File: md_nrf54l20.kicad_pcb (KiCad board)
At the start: 4 copper layers, 43.2 x 17.8 mm, 42 parts, among them J10 Conn_01x15, J5 USB_C, J7 JST SH I2C, J9 Conn_01x15, SW1 RESET, U1 nRF54L20, U2 AMS1117-3.3, U3 CH347T, U4 M6017-02, Y1 8MHz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

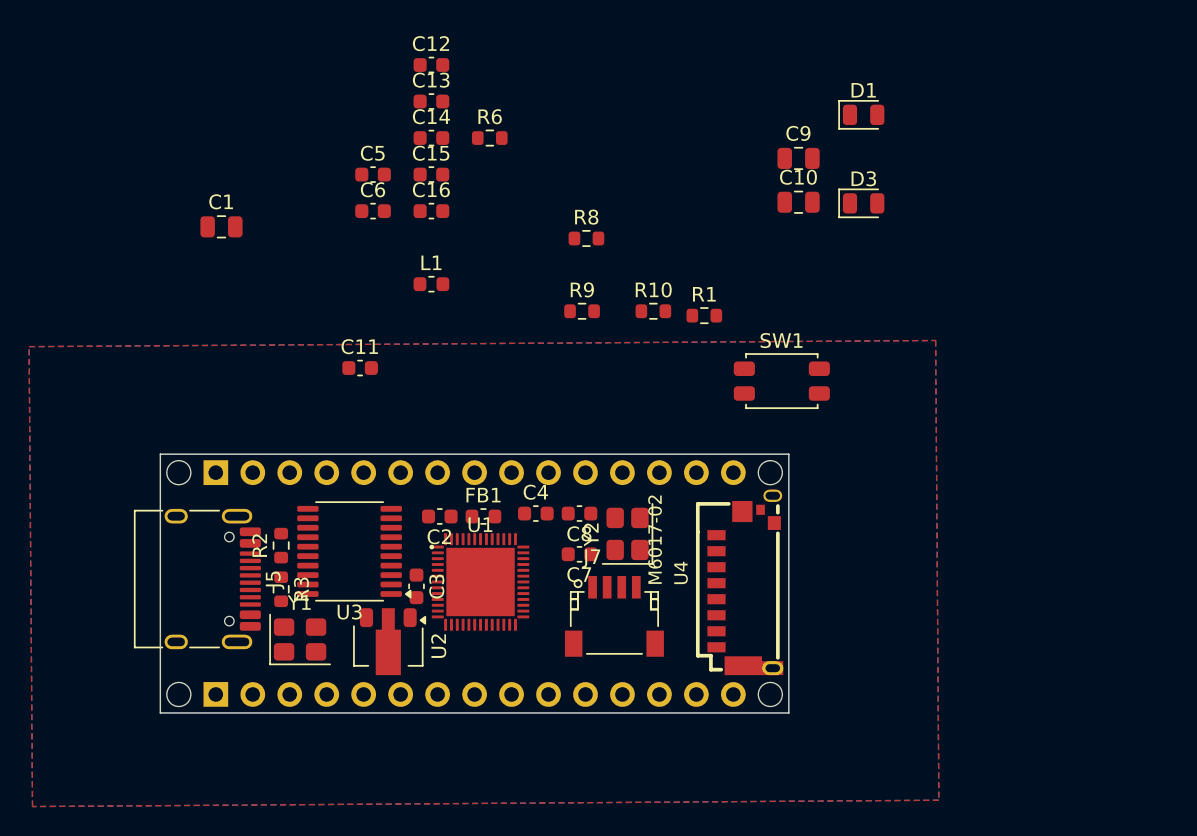
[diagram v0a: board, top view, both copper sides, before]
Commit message: Remove 10uf filter cap
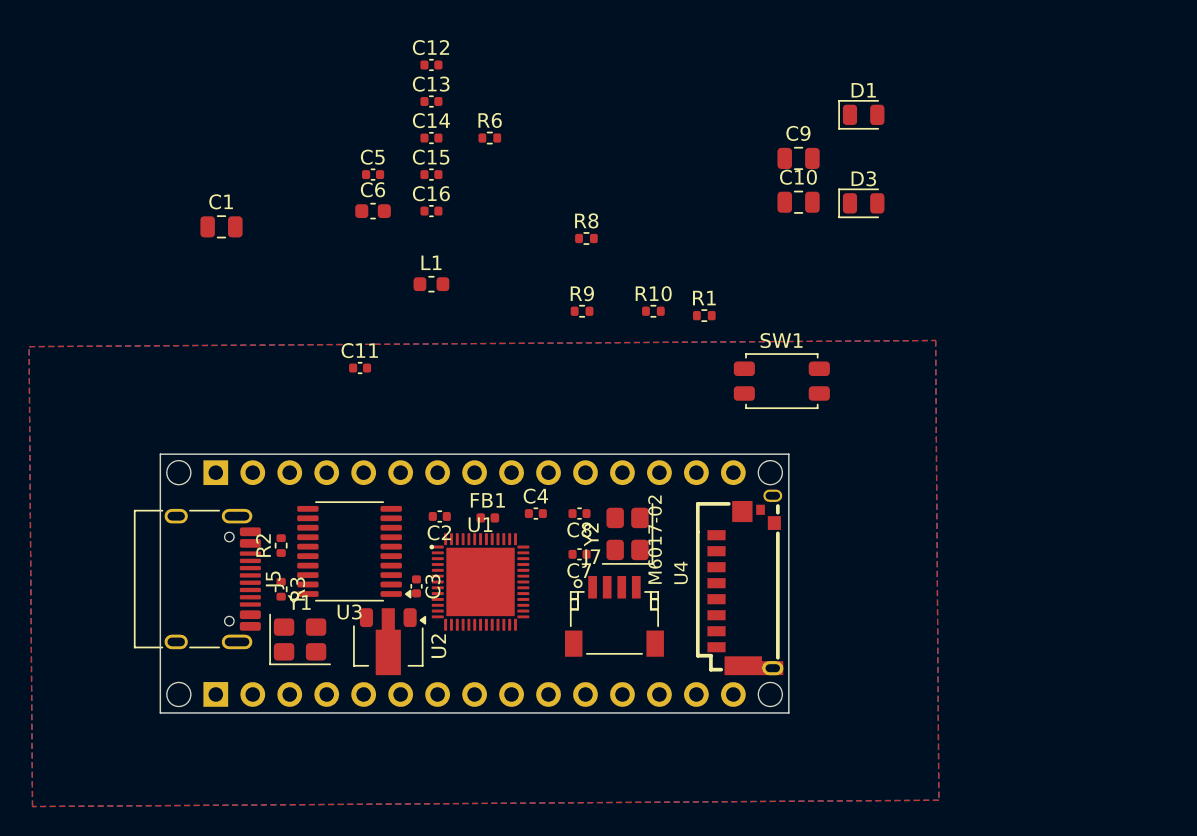
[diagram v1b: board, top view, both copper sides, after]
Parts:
- C11, C12, C13, C14, C15, C16, C2, C3, C4, C5, C7, C8: footprint Capacitor_SMD:C_0603_1608Metric -> Capacitor_SMD:C_0402_1005Metric
- FB1: footprint Inductor_SMD:L_0603_1608Metric -> Inductor_SMD:L_0402_1005Metric
- R1, R10, R2, R3, R6, R8, R9: footprint Resistor_SMD:R_0603_1608Metric -> Resistor_SMD:R_0402_1005Metric
- moved FB1 0.32 mm to (122.5, 86.6)

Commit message: Layout work
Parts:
- removed C1: 10uF, Capacitor_SMD:C_0805_2012Metric
- moved C9 39.5 mm to (123.3, 95.6)
- moved C12 39.0 mm to (109.2, 93.3), turned to 180 degrees
- moved C10 36.1 mm to (118.2, 90.3), turned to 180 degrees
- moved C13 35.4 mm to (115.4, 93.2)
- moved R10 22.6 mm to (112.7, 80.2)
- moved R9 22.6 mm to (107.8, 80.2)
- moved C11 12.1 mm to (108.1, 87.0), turned to 90 degrees
- moved L1 11.5 mm to (127.1, 78.3)
- moved U2 3.70 mm to (119.0, 93.8), turned to 90 degrees
- moved C3 3.51 mm to (120.9, 90.1), turned to 90 degrees
- moved C2 3.42 mm to (122.6, 86.9)
- moved U1 3.10 mm to (125.1, 91.0)
- moved FB1 2.92 mm to (125.4, 86.6)
- moved Y1 2.70 mm to (112.3, 94.9)
- moved C4 1.63 mm to (127.4, 86.6)
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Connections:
- U1 pad 25: unconnected-(U1-P0.03-Pad25) -> /CH_UART_RX
- U1 pad 50: unconnected-(U1-P1.24-Pad50) -> /CH_UART_TX
- U3 pad 3: unconnected-(U3-TXD1-Pad3) -> /CH_UART_TX
- U3 pad 4: unconnected-(U3-RXD1-Pad4) -> /CH_UART_RX

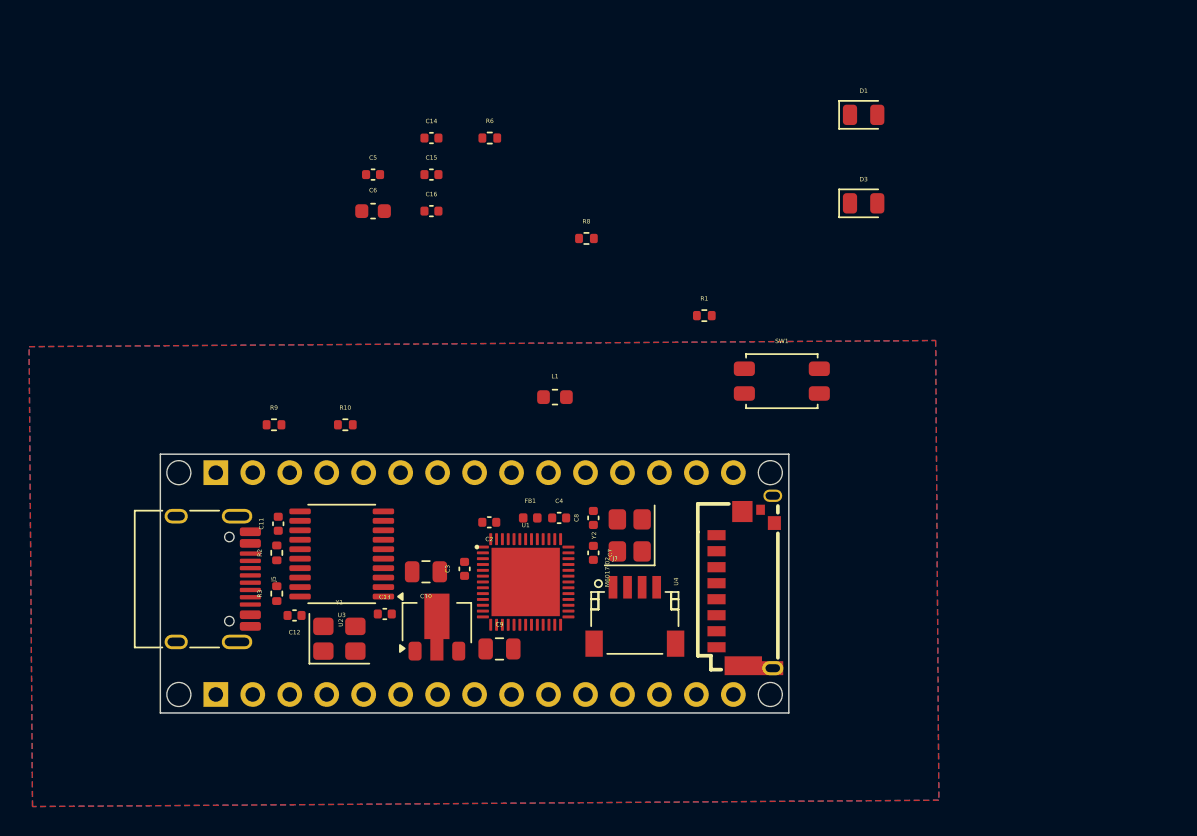
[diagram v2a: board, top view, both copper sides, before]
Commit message: Layout work, all main components on board
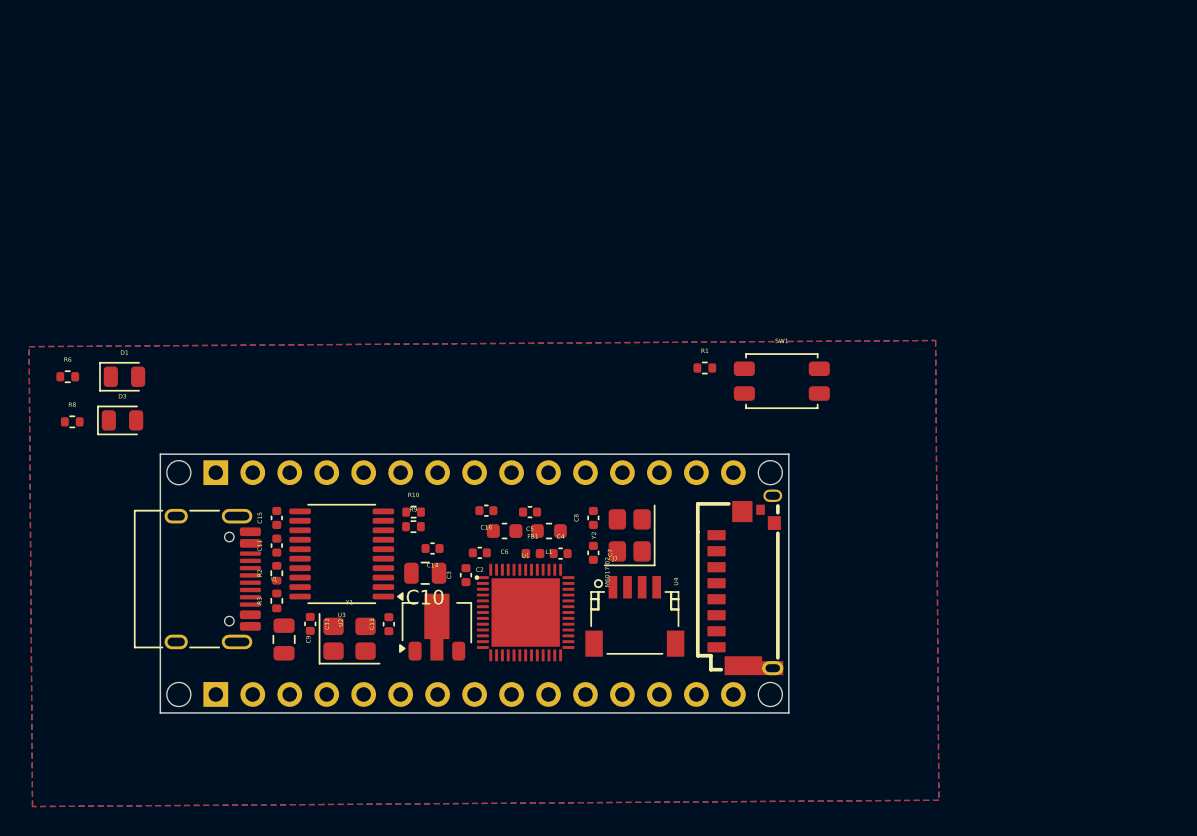
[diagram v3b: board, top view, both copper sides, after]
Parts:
- C10: value 22uF -> 10uF
- moved D1 53.9 mm to (97.5, 76.9)
- moved D3 53.1 mm to (97.4, 79.9)
- moved R8 37.5 mm to (93.9, 80.0)
- moved R6 33.3 mm to (93.6, 76.9)
- moved C14 28.2 mm to (118.7, 88.7), turned to 180 degrees
- moved C15 25.9 mm to (108.0, 86.6), turned to 90 degrees
- moved C5 25.6 mm to (125.4, 86.2), turned to 180 degrees
- moved C6 23.8 mm to (123.7, 87.5), turned to 180 degrees
- moved C16 20.9 mm to (122.4, 86.1), turned to 180 degrees
- moved C9 14.8 mm to (108.5, 95.0), turned to -90 degrees
- moved R9 11.9 mm to (117.4, 87.2)
- moved L1 9.21 mm to (126.7, 87.5), turned to 180 degrees
- moved R10 7.62 mm to (117.4, 86.2)
- moved R1 3.60 mm to (137.4, 76.3)
- moved FB1 2.46 mm to (125.6, 89.0)
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
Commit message: Pre-flip routing
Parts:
- moved J7 16.5 mm to (148.6, 88.9), turned to 180 degrees
- moved R3 11.8 mm to (96.2, 93.0), turned to 0 degrees
- moved C16 11.6 mm to (130.8, 94.0)
- moved C13 7.61 mm to (108.1, 94.0), turned to -90 degrees
- moved C9 6.95 mm to (115.5, 95.0)
- moved Y2 3.63 mm to (131.8, 91.4)
- moved C8 3.61 mm to (129.5, 90.2)
- moved SW1 3.15 mm to (145.3, 78.9)
- moved C7 3.11 mm to (129.5, 92.1)
- moved C12 3.10 mm to (113.4, 94.0)
- moved FB1 2.72 mm to (123.0, 88.1), turned to 90 degrees
- moved C6 2.66 mm to (121.0, 87.8)
- moved Y1 2.26 mm to (110.7, 94.9), turned to 180 degrees
- moved L1 1.70 mm to (125.0, 87.9)
- moved R2 1.40 mm to (108.0, 91.8)
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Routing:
- net Net-(U1-DECRF): track 0.00 -> 24.6 mm
- net +3V3: track 0.00 -> 16.1 mm
- net Net-(U3-XI): track 0.00 -> 7.09 mm
- net Net-(U3-XO): track 0.00 -> 6.04 mm
- net Net-(U1-XC1): track 0.00 -> 5.76 mm
- net Net-(U1-DECA): track 0.00 -> 5.68 mm
- net Net-(U1-XC2): track 0.00 -> 4.92 mm
- net Net-(U1-DECD): track 0.00 -> 4.53 mm
- net /USB_DN: track 0.00 -> 3.56 mm
- net /USB_DP: track 0.00 -> 3.50 mm
- net VBUS: track 0.00 -> 3.46 mm
- net Net-(U1-DCC): track 0.00 -> 2.46 mm
- net /D10_CS: track 0.00 -> 2.08 mm, vias 0 -> 1
- net /SWDCLK: track 0.00 -> 2.06 mm, vias 0 -> 1
- net /D9_PWM: track 0.00 -> 2.06 mm, vias 0 -> 1
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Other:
- board text added: "swap to vertical"

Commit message: Post flip routing
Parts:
- moved C9 22.0 mm to (136.1, 87.4), turned to 90 degrees
- moved U2 15.1 mm to (132.6, 87.9), turned to 90 degrees
- moved C14 14.9 mm to (132.9, 93.2), turned to 0 degrees
- moved C10 14.6 mm to (133.1, 91.8), turned to 0 degrees
- moved Y2 13.1 mm to (118.7, 91.2), turned to -90 degrees
- moved C16 12.4 mm to (119.7, 88.5), turned to 0 degrees
- moved C6 11.1 mm to (129.5, 94.8), turned to 0 degrees
- moved C5 9.34 mm to (125.8, 95.9), turned to 180 degrees
- moved C2 8.82 mm to (129.1, 93.5), turned to 0 degrees
- moved C8 8.77 mm to (121.0, 92.4), turned to -90 degrees
- moved C7 8.65 mm to (121.0, 90.5), turned to 90 degrees
- moved C3 8.53 mm to (129.5, 90.7), turned to -90 degrees
- moved FB1 7.75 mm to (127.5, 94.5), turned to -90 degrees
- moved C4 7.09 mm to (123.0, 94.0), turned to 180 degrees
- moved L1 6.80 mm to (125.5, 94.7), turned to 0 degrees
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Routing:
- net +3V3: track 16.1 -> 13.2 mm

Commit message: More routing
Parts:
- moved C3 0.86 mm to (129.9, 90.0)
- moved C10 0.37 mm to (133.4, 91.7)
- moved C14 0.37 mm to (133.3, 93.1)
- moved C9 0.37 mm to (136.5, 87.3)
- moved U2 0.37 mm to (133.0, 87.8)
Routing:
- net /A5_SCL: track 0.89 -> 20.3 mm
- net /SD_CS: track 0.00 -> 17.1 mm, vias 0 -> 2
- net /SD_MOSI: track 0.00 -> 16.4 mm, vias 0 -> 2
- net /A4_SDA: track 0.76 -> 17.1 mm, vias 1 -> 2
- net /SD_SCK: track 0.00 -> 13.3 mm
- net /A3: track 0.90 -> 13.1 mm
- net /A0: track 1.23 -> 13.4 mm
- net /SD_MISO: track 0.00 -> 11.9 mm
- net /A2: track 1.12 -> 12.8 mm
- net /A1: track 1.59 -> 12.8 mm
- net unconnected-(U1-P2.03-Pad3): track 0.00 -> 7.95 mm, vias 0 -> 1
- net /D4: track 0.99 -> 6.43 mm, vias 1 -> 0
- net /D8: track 0.61 -> 4.30 mm
- net /D7: track 0.35 -> 4.00 mm
- net /D5_PWM: track 0.91 -> 4.40 mm, vias 1 -> 0
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
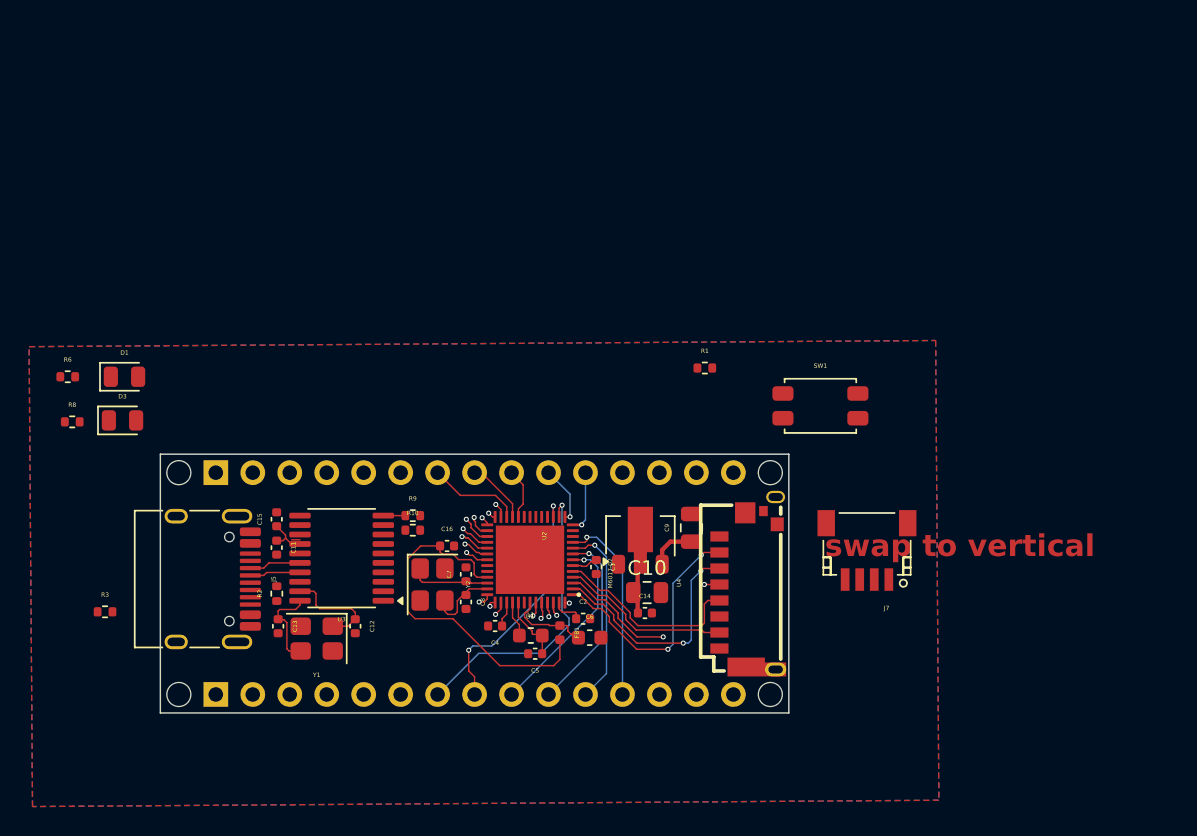
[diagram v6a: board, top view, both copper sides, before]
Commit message: More routing, swap jst sh to vertical
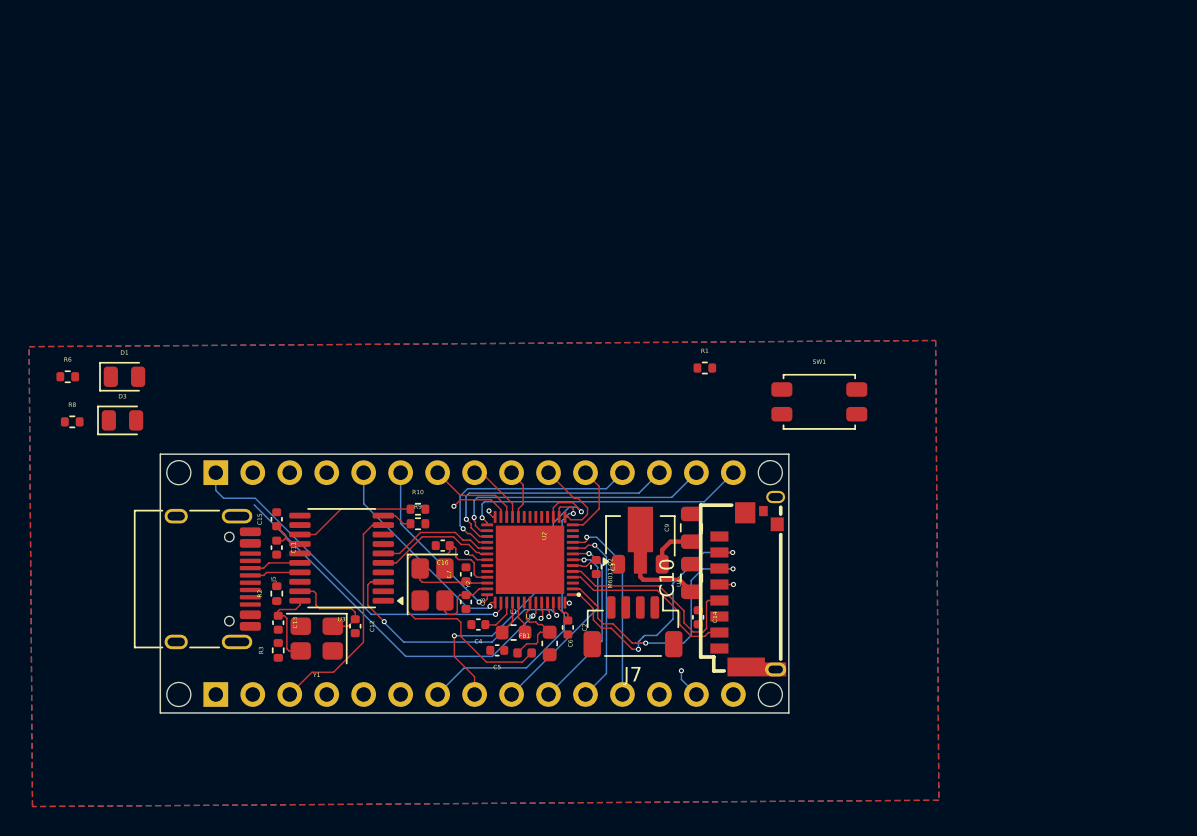
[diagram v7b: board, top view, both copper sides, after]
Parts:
- J7: footprint Connectors_JST:JST_SH_SM04B-SRSS-TB_04x1.00mm_Angled -> Connector_JST:JST_SH_BM04B-SRSS-TB_1x04-1MP_P1.00mm_Vertical
- moved J7 16.9 mm to (132.5, 94.1)
- moved R3 12.2 mm to (108.1, 95.7), turned to 90 degrees
- moved C14 3.67 mm to (136.9, 93.4), turned to -90 degrees
- moved C10 3.22 mm to (136.5, 90.7), turned to 90 degrees
- moved FB1 2.80 mm to (125.0, 95.9), turned to 0 degrees
- moved C6 2.78 mm to (126.8, 95.2), turned to -90 degrees
- moved C5 2.62 mm to (123.1, 95.7)
- moved R10 1.48 mm to (117.7, 86.0)
- moved C2 1.21 mm to (128.0, 94.1), turned to -90 degrees
- moved L1 1.20 mm to (124.3, 94.5)
- moved C4 1.15 mm to (121.8, 93.9)
- moved R9 0.66 mm to (117.7, 87.0)
- moved C16 0.30 mm to (119.4, 88.5), turned to 180 degrees
- moved SW1 0.29 mm to (145.3, 78.6)
- moved C13 0.24 mm to (108.1, 93.8)
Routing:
- net /D0_RX: track 0.99 -> 25.6 mm
- net /D1_TX: track 1.04 -> 25.0 mm
- net /D12_CITO: track 0.64 -> 19.7 mm
- net /CH_UART_TX: track 0.97 -> 18.7 mm, vias 1 -> 2
- net /D11_COTI: track 1.55 -> 18.8 mm
- net /nRESET: track 1.62 -> 17.2 mm
- net /D10_CS: track 2.08 -> 17.6 mm
- net /D9_PWM: track 2.06 -> 16.2 mm
- net /D2: track 0.72 -> 14.6 mm
- net /D3_PWM: track 0.94 -> 12.1 mm
- net /MODE_R: track 0.00 -> 8.33 mm
- net unconnected-(U1-P2.03-Pad3): track 7.95 -> 0.00 mm, vias 1 -> 0
- net /SWDIO: track 1.82 -> 8.37 mm, vias 1 -> 0
- net /SWDCLK: track 2.06 -> 8.18 mm, vias 1 -> 0
- net /A4_SDA: track 17.1 -> 22.2 mm
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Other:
- board text removed: "swap to vertical"

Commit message: Update layout
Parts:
- added D4: G_LED, LED_SMD:LED_0402_1005Metric, F.Cu at (114.5, 93.8)
- added D5: O_LED, LED_SMD:LED_0402_1005Metric, F.Cu at (113.5, 93.8)
- added J1: U.FL Conn, Connector_Coaxial:U.FL_Hirose_U.FL-R-SMT-1_Vertical, F.Cu at (118.1, 89.2)
- added R11: 220, Resistor_SMD:R_0402_1005Metric, F.Cu at (113.5, 95.8)
- added R12: 220, Resistor_SMD:R_0402_1005Metric, F.Cu at (114.5, 95.8)
- D1, D3: footprint LED_SMD:LED_0805_2012Metric -> LED_SMD:LED_0402_1005Metric
- Y1, Y2: footprint Crystal:Crystal_SMD_3225-4Pin_3.2x2.5mm -> Crystal:Crystal_SMD_2016-4Pin_2.0x1.6mm
- moved R8 28.5 mm to (117.8, 95.7), turned to 180 degrees
- moved D3 27.3 mm to (119.7, 95.7)
- moved R6 25.3 mm to (110.0, 96.2)
- moved D1 24.1 mm to (112.0, 96.2)
- moved R1 3.04 mm to (140.0, 77.9)
- moved C16 2.88 mm to (120.5, 91.2), turned to -90 degrees
- moved C7 2.78 mm to (120.3, 93.2), turned to -90 degrees
- moved Y2 2.09 mm to (118.4, 93.2)
- moved R10 1.80 mm to (119.5, 86.0)
- moved R2 1.68 mm to (108.0, 90.1), turned to -90 degrees
- moved C12 1.15 mm to (112.2, 93.9)
- moved R9 1.01 mm to (117.6, 86.0)
- moved C8 0.85 mm to (121.3, 93.2)
- moved Y1 0.82 mm to (110.2, 94.3)
- moved C4 0.69 mm to (122.5, 94.3), turned to -90 degrees
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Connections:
- U1 pad 34: unconnected-(U1-ANT-Pad34) -> Net-(J1-In)
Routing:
- net /D13_SCK: track 0.72 -> 26.8 mm
- net /CH_UART_RX: track 4.20 -> 22.5 mm, vias 1 -> 2
- net /nRESET: track 17.2 -> 27.8 mm, vias 1 -> 2
- net VBUS: track 3.46 -> 10.8 mm
- net +3V3: track 19.2 -> 24.1 mm, vias 2 -> 7
- net Net-(J5-CC2): track 0.00 -> 4.88 mm
- net Net-(U1-DECRF): track 22.1 -> 17.8 mm
- net Net-(J1-In): track 0.00 -> 3.12 mm
- net /MODE_R: track 8.33 -> 11.3 mm
- net /A4_SDA: track 22.2 -> 19.5 mm, vias 2 -> 1
- net /USB_DN: track 3.56 -> 0.91 mm
- net /SWDIO: track 8.37 -> 10.6 mm
- net Net-(U1-DECD): track 2.25 -> 4.37 mm
- net /SWDCLK: track 8.18 -> 10.2 mm
- net Net-(U3-XI): track 7.09 -> 5.09 mm
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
